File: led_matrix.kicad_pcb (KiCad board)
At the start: 2 copper layers, 85.1 x 109.2 mm, 116 parts, among them J1 I2C, J2 Extra, J3 Address, J4 +5V, J5 GND, J6 Power Input, J7 Columns, J8 Row Addr., Q1 2N3904, Q2 2N3904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

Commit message: Update PCB
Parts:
- R17, R18: value 1K -> DNF
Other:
- board text added: "COLUMNS"
- board text added: "Columns:"
- board text added: "ROW Address:"
- board text added: "ROWS"
- board text removed: "Columns"
- board text removed: "ROW Address"
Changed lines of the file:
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@@
 		)
 		(property "Value" "100nF"
-			(at 2.5 2.5 0)
-			(layer "F.Fab")
+			(at 2.5 0 0)
+			(layer "F.SilkS")
 			(effects
 				(font
-					(size 1 1)
-					(thickness 0.15)
+					(size 0.7 0.7)
+					(thickness 0.1)
 				)
 			)
@@
 		)
 		(property "Value" "100nF"
-			(at 2.5 2.5 0)
-			(layer "F.Fab")
+			(at 2.5 0 0)
+			(layer "F.SilkS")
 			(effects
 				(font
-					(size 1 1)
-					(thickness 0.15)
+					(size 0.7 0.7)
+					(thickness 0.1)
 				)
 			)
@@
 		(tags "Through hole pin header THT 1x02 2.54mm single row")
 		(property "Reference" "J1"
-			(at -1.131714 5.411572 180)
+			(at -0.369714 5.411572 180)
 			(layer "F.SilkS")
 			(effects
@@
 			)
 		)
-		(property "Value" "1K"
+		(property "Value" "DNF"
 			(at 5.08 0 90)
-			(layer "F.Fab")
+			(layer "F.SilkS")
 			(effects
 				(font
@@
 		(tags "Through hole pin header THT 1x03 2.54mm single row")
 		(property "Reference" "J2"
-			(at 0.115714 -2.668372 180)
+			(at 0.369714 -2.668372 180)
 			(layer "F.SilkS")
 			(effects
@@
 			)
 		)
-		(property "Value" "1K"
+		(property "Value" "DNF"
 			(at 5.08 0 90)
-			(layer "F.Fab")
+			(layer "F.SilkS")
 			(effects
 				(font
@@
 		)
 		(property "Value" "100nF"
-			(at 2.5 2.5 90)
-			(layer "F.Fab")
+			(at 2.5 0 90)
+			(layer "F.SilkS")
 			(effects
 				(font
-					(size 1 1)
-					(thickness 0.15)
+					(size 0.7 0.7)
+					(thickness 0.1)
 				)
 			)
@@
 		)
 		(property "Value" "100nF"
-			(at 2.5 2.5 0)
-			(layer "F.Fab")
+			(at 2.5 0 0)
+			(layer "F.SilkS")
 			(effects
 				(font
-					(size 1 1)
-					(thickness 0.15)
+					(size 0.7 0.7)
+					(thickness 0.1)
 				)
 			)
@@
 		)
 	)
-	(gr_text "Columns"
-		(at 136.652 60.198 0)
+	(gr_text "Columns:"
+		(at 136.398 60.198 0)
 		(layer "F.SilkS")
 		(effects
 			(font
 				(size 1 1)
-				(thickness 0.1)
+				(thickness 0.2)
+				(bold yes)
 			)
 			(justify left bottom)
@@
 		)
 	)
+	(gr_text "ROWS"
+		(at 182.626 115.062 90)
+		(layer "F.SilkS")
+		(effects
+			(font
+				(size 1 2)
+				(thickness 0.2)
+				(bold yes)
+			)
+		)
+	)
 	(gr_text "7"
 		(at 152.4 61.722 0)
@@
 		)
 	)
+	(gr_text "COLUMNS"
+		(at 148.082 149.86 0)
+		(layer "F.SilkS")
+		(effects
+			(font
+				(size 1 2)
+				(thickness 0.2)
+				(bold yes)
+			)
+		)
+	)
 	(gr_text "+"
 		(at 109.728 44.704 0)
@@
 			(font
 				(size 1 1)
-				(thickness 0.1)
+				(thickness 0.2)
+				(bold yes)
 			)
 		)
@@
 	)
 	(gr_text "SCK|SDA ->"
-		(at 146.095572 45.327714 0)
+		(at 146.095572 46.089714 0)
 		(layer "F.SilkS")
 		(effects
@@
 		)
 	)
-	(gr_text "ROW\nAddress"
-		(at 108.005572 67.403714 0)
+	(gr_text "ROW Address:"
+		(at 104.648 71.882 90)
 		(layer "F.SilkS")
 		(effects
 			(font
 				(size 1 1)
-				(thickness 0.1)
+				(thickness 0.2)
+				(bold yes)
 			)
-			(justify right bottom)
 		)
 	)

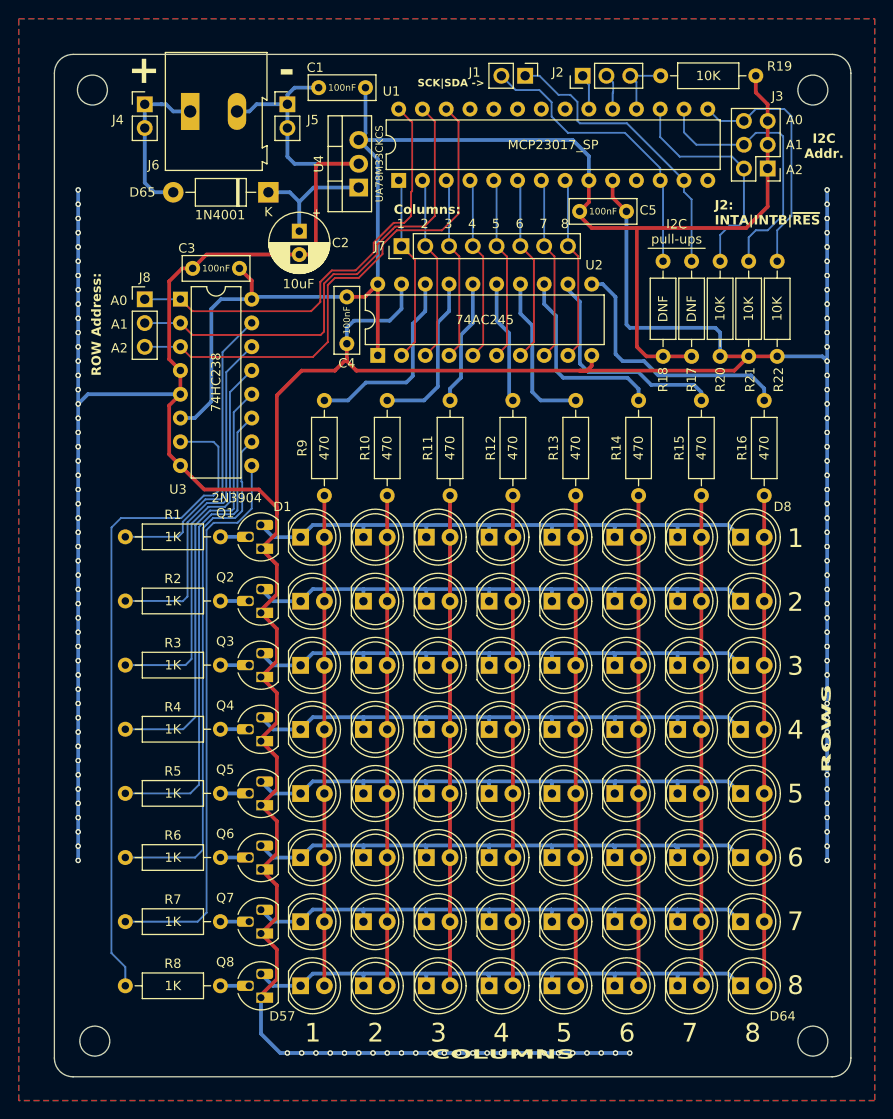
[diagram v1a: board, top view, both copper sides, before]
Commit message: Update silkscreen a bit
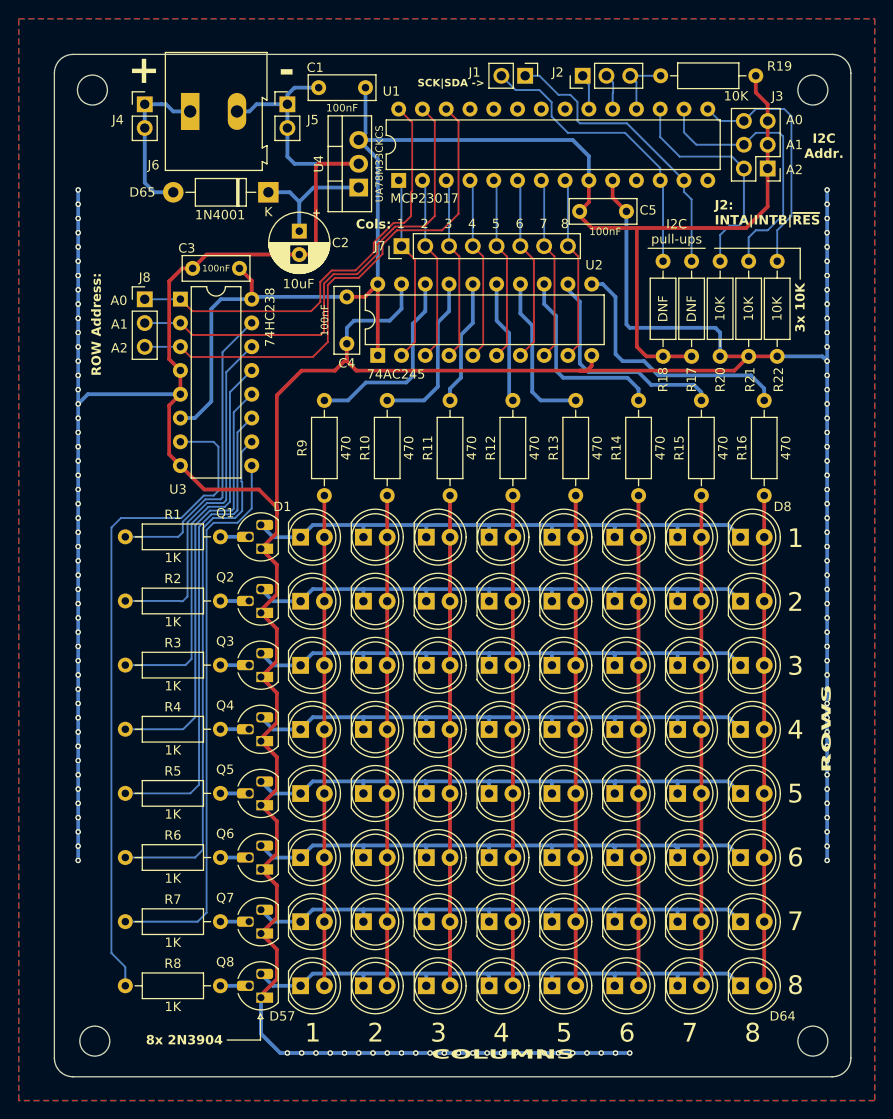
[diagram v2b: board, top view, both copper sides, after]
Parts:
- U1: value MCP23017_SP -> MCP23017
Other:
- board text added: "3x 10K"
- board text added: "8x 2N3904"
- board text added: "Cols:"
- board text removed: "Columns:"
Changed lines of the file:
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@@
 			(outputformat 1)
 			(mirror no)
-			(drillshape 1)
+			(drillshape 0)
 			(scaleselection 1)
-			(outputdirectory "")
+			(outputdirectory "gerbers/")
 		)
 	)
@@
 		)
 		(property "Value" "100nF"
-			(at 2.5 0 0)
+			(at 2.737228 2.160286 0)
 			(layer "F.SilkS")
 			(effects
 				(font
-					(size 0.7 0.7)
+					(size 0.8 0.8)
 					(thickness 0.1)
 				)
@@
 		)
 		(property "Value" "10K"
-			(at 5.08 0 0)
+			(at 2.109572 -2.170286 0)
 			(layer "F.SilkS")
 			(effects
@@
 		)
 		(property "Value" "74AC245"
-			(at 3.8 11.425 180)
+			(at -2.015375 1.954428 180)
 			(layer "F.SilkS")
 			(effects
@@
 		)
 		(property "Value" "1K"
-			(at 5.08 0 0)
+			(at 5.08 2.238 0)
 			(layer "F.SilkS")
 			(effects
@@
 		)
 		(property "Value" "1K"
-			(at 5.08 0 0)
+			(at 5.08 2.238 0)
 			(layer "F.SilkS")
 			(effects
@@
 			)
 		)
-		(property "Value" "MCP23017_SP"
-			(at 3.8 16.5 180)
+		(property "Value" "MCP23017"
+			(at -1.916286 2.767228 180)
 			(layer "F.SilkS")
 			(effects
@@
 		)
 		(property "Value" "470"
-			(at 5.08 0 90)
+			(at 5.08 2.322285 90)
 			(layer "F.SilkS")
 			(effects
@@
 		)
 		(property "Value" "470"
-			(at 5.08 0 90)
+			(at 5.08 2.322285 90)
 			(layer "F.SilkS")
 			(effects
@@
 		)
 		(property "Value" "1K"
-			(at 5.08 0 0)
+			(at 5.08 2.238 0)
 			(layer "F.SilkS")
 			(effects
@@
 		)
 		(property "Value" "1K"
-			(at 5.08 0 0)
+			(at 5.08 2.238 0)
 			(layer "F.SilkS")
 			(effects
@@
 		)
 		(property "Value" "470"
-			(at 5.08 0 90)
+			(at 5.08 2.322285 90)
 			(layer "F.SilkS")
 			(effects
@@
 		)
 		(property "Value" "470"
-			(at 5.08 0 90)
+			(at 5.08 2.322285 90)
 			(layer "F.SilkS")
 			(effects
@@
 		)
 		(property "Value" "1K"
-			(at 5.08 0 0)
+			(at 5.08 2.238 0)
 			(layer "F.SilkS")
 			(effects
@@
 		)
 		(property "Value" "470"
-			(at 5.08 0 90)
+			(at 5.08 2.322285 90)
 			(layer "F.SilkS")
 			(effects
@@
 		)
 		(property "Value" "1K"
-			(at 5.08 0 0)
+			(at 5.08 2.238 0)
 			(layer "F.SilkS")
 			(effects
@@
 			(at 5.427142 -2.588286 180)
 			(layer "F.SilkS")
+			(hide yes)
 			(effects
 				(font
@@
 		)
 		(property "Value" "470"
-			(at 5.08 0 90)
+			(at 5.08 2.322285 90)
 			(layer "F.SilkS")
 			(effects
@@
 		)
 		(property "Value" "74HC238"
-			(at 3.8 8.875 90)
+			(at 9.574428 1.931286 90)
 			(layer "F.SilkS")
 			(effects
@@
 		)
 		(property "Value" "470"
-			(at 5.08 0 90)
+			(at 5.08 2.322285 90)
 			(layer "F.SilkS")
 			(effects
@@
 		)
 		(property "Value" "470"
-			(at 5.08 0 90)
+			(at 5.08 2.322285 90)
 			(layer "F.SilkS")
 			(effects
@@
 		)
 		(property "Value" "100nF"
-			(at 2.5 0 90)
+			(at 2.5 2.363572 90)
 			(layer "F.SilkS")
 			(effects
 				(font
-					(size 0.7 0.7)
+					(size 0.8 0.8)
 					(thickness 0.1)
 				)
@@
 		)
 		(property "Value" "1K"
-			(at 5.08 0 0)
+			(at 5.08 2.238 0)
 			(layer "F.SilkS")
 			(effects
@@
 		)
 		(property "Value" "100nF"
-			(at 2.5 0 0)
+			(at 2.5 -2.170286 0)
 			(layer "F.SilkS")
 			(effects
 				(font
-					(size 0.7 0.7)
+					(size 0.8 0.8)
 					(thickness 0.1)
 				)
@@
 		)
 		(property "Value" "1K"
-			(at 5.08 0 0)
+			(at 5.08 2.238 0)
 			(layer "F.SilkS")
 			(effects
@@
 	)
 	(gr_line
+		(start 122.174 145.542)
+		(end 121.92 146.05)
+		(stroke
+			(width 0.1)
+			(type default)
+		)
+		(layer "F.SilkS")
+	)
+	(gr_line
+		(start 170.688 63.754)
+		(end 179.832 63.754)
+		(stroke
+			(width 0.1)
+			(type default)
+		)
+		(layer "F.SilkS")
+	)
+	(gr_line
+		(start 122.174 148.336)
+		(end 122.174 146.05)
+		(stroke
+			(width 0.1)
+			(type default)
+		)
+		(layer "F.SilkS")
+	)
+	(gr_line
 		(start 163.576 63.754)
 		(end 169.672 63.754)
@@
 		(layer "F.SilkS")
 	)
+	(gr_line
+		(start 121.92 146.05)
+		(end 122.428 146.05)
+		(stroke
+			(width 0.1)
+			(type default)
+		)
+		(layer "F.SilkS")
+	)
+	(gr_line
+		(start 118.618 148.336)
+		(end 122.174 148.336)
+		(stroke
+			(width 0.1)
+			(type default)
+		)
+		(layer "F.SilkS")
+	)
+	(gr_line
+		(start 179.832 63.754)
+		(end 179.832 67.056)
+		(stroke
+			(width 0.1)
+			(type default)
+		)
+		(layer "F.SilkS")
+	)
+	(gr_line
+		(start 122.428 146.05)
+		(end 122.174 145.542)
+		(stroke
+			(width 0.1)
+			(type default)
+		)
+		(layer "F.SilkS")
+	)
 	(gr_arc
 		(start 183.243572 43.041714)
@@
 		)
 	)
-	(gr_text "Columns:"
-		(at 136.398 60.198 0)
+	(gr_text "Cols:"
+		(at 136.144 61.1825 0)
 		(layer "F.SilkS")
 		(effects
@@
 				(bold yes)
 			)
-			(justify left bottom)
+			(justify right)
 		)
 	)
@@
 		)
 	)
+	(gr_text "3x 10K"
+		(at 179.832 70.104 90)
+		(layer "F.SilkS")
+		(effects
+			(font
+				(size 1 1)
+				(thickness 0.2)
+				(bold yes)
+			)
+		)
+	)
 	(gr_text "A2"
 		(at 108.005572 74.422 0)
@@
 			)
 		)
+	)
+	(gr_text "8x 2N3904"
+		(at 114.046 148.336 0)
+		(layer "F.SilkS")
+		(effects
+			(font
+				(size 1 1)
+				(thickness 0.2)
+				(bold yes)
+			)
+		)
